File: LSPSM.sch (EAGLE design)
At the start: 164 parts, among them IC1 ATmega328P, IC10 TMP102, IC11 TMP102, IC2 ATMEGA16U2-MU, IC3 LTC3115, IC4 LTC4078, IC5 MAX17043G+U, IC6 MAX4372F, IC7 LTC3536, IC8 MAX4372F, IC9 LTC3536, Q1 RJU003N03 N-MOSFET, Q2 RJU003N03 N-MOSFET, Q4 RJU003N03 N-MOSFET, Q5 RJU003N03 N-MOSFET, Q6 RJU003N03 N-MOSFET, Q7 RJU003N03 N-MOSFET, Q8 RJU003N03 N-MOSFET, Q9 RJU003N03 N-MOSFET, SW1 RESET, SW2 SWITCH-SPDT

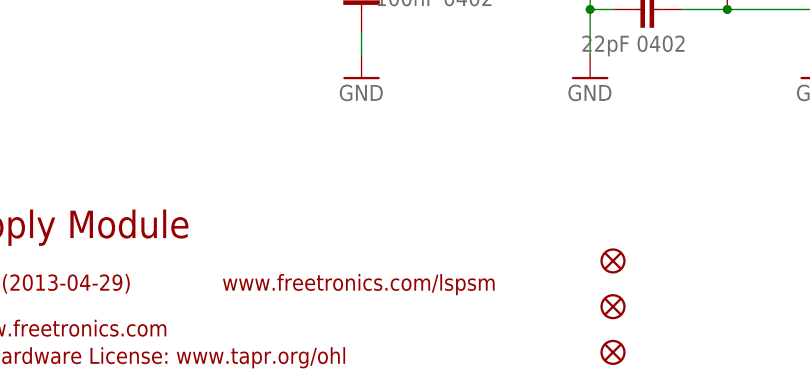
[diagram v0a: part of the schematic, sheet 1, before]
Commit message: Removed ArduSat logo from silkscreen
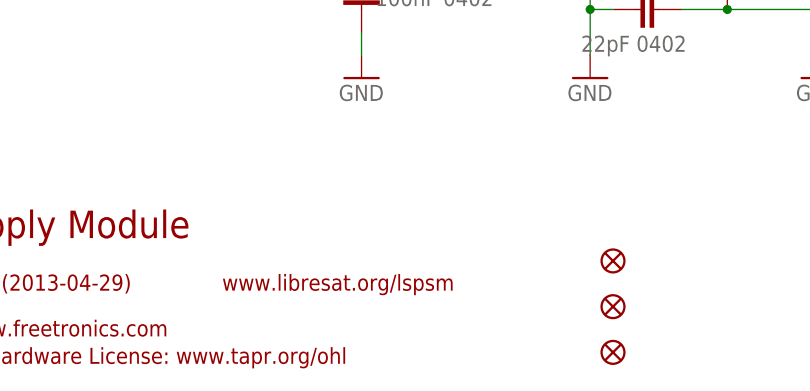
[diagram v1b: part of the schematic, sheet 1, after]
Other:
- note added: "www.libresat.org/lspsm"
- note removed: "www.freetronics.com/lspsm"
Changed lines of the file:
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@@
 <text x="7.366" y="9.398" size="1.778" layer="94">(C)2013 Freetronics Pty Ltd: www.freetronics.com</text>
 <text x="7.366" y="6.35" size="1.778" layer="94">Licensed under the TAPR Open Hardware License: www.tapr.org/ohl</text>
-<text x="68.326" y="14.478" size="1.778" layer="94">www.freetronics.com/lspsm</text>
+<text x="68.326" y="14.478" size="1.778" layer="94">www.libresat.org/lspsm</text>
 <frame x1="5.08" y1="12.7" x2="109.22" y2="25.4" columns="0" rows="0" layer="94" border-left="no" border-top="no" border-right="no" border-bottom="no"/>
 <frame x1="5.08" y1="12.7" x2="35.56" y2="17.78" columns="8" rows="5" layer="94"/>
